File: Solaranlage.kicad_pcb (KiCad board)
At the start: 2 copper layers, 160 x 85 mm, 87 parts, among them J1 Screw_Terminal_01x02, J2 Screw_Terminal_01x02, J3 AVR-JTAG-10, J4 USB_B, J5 USB_B, J6 Screw_Terminal_01x02, Q1 2N3904, SW1 Rotary_Encoder_Switch_Panason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, SW2 SW_SPDT, U1 SC56-11E*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

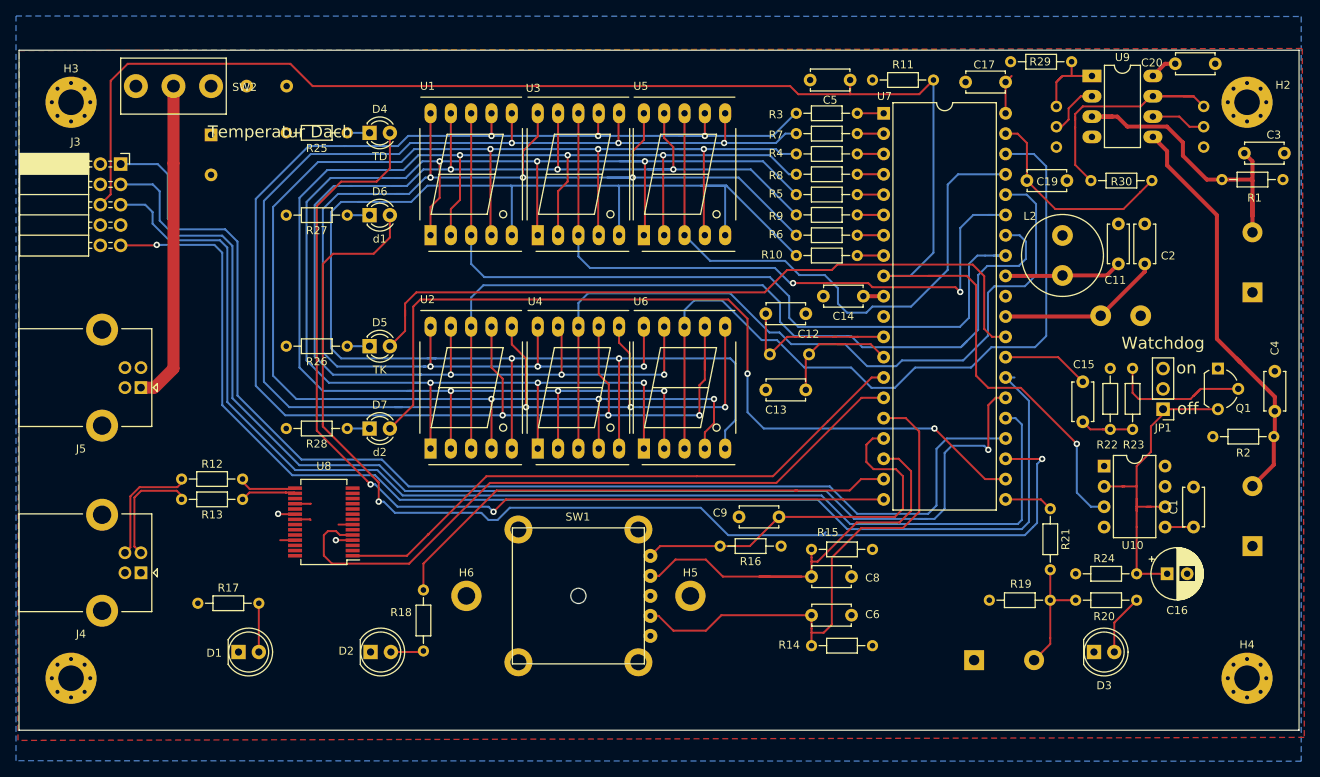
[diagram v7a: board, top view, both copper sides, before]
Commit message: adapted remarks from schematic review; added output buffer to PWM output
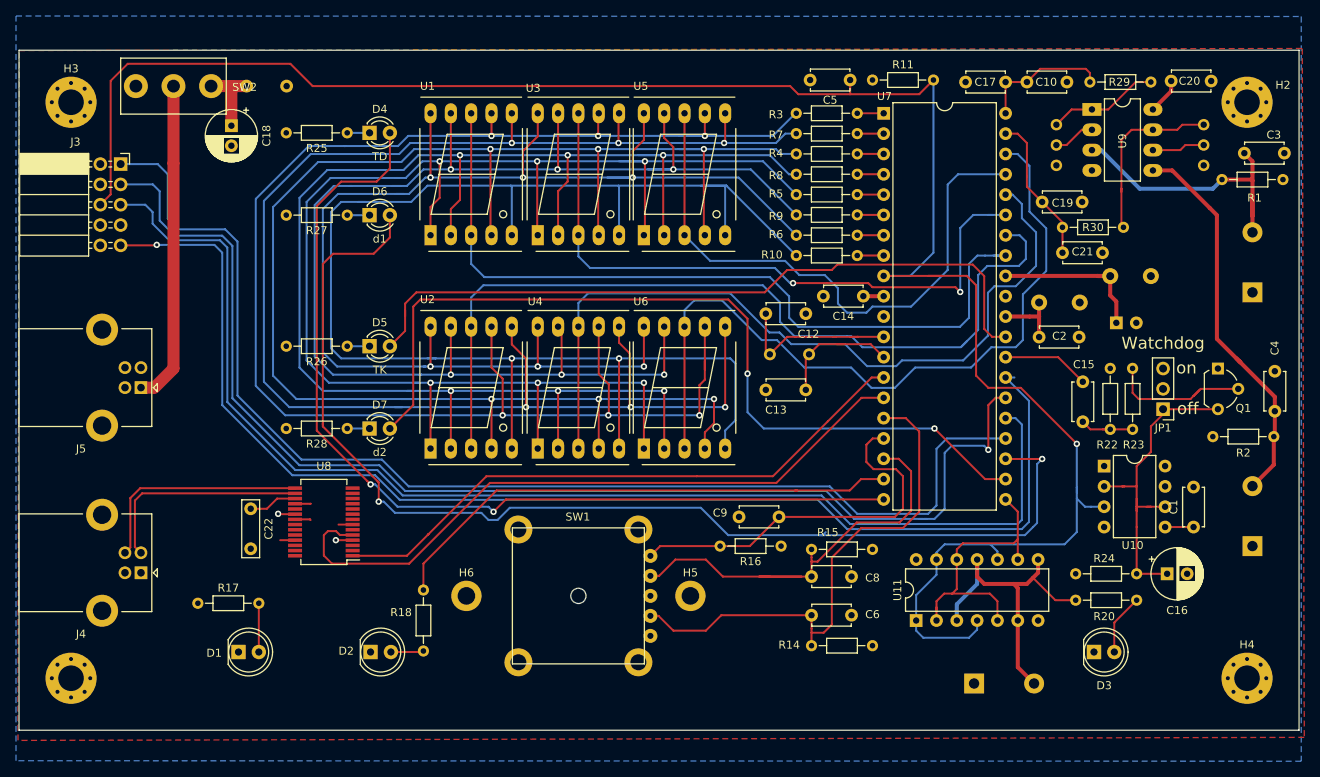
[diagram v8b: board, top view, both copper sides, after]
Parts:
- removed R12, R13: 22, Resistor_THT:R_Axial_DIN0204_L3.6mm_D1.6mm_P7.62mm_Horizontal
- removed R19: 10k, Resistor_THT:R_Axial_DIN0204_L3.6mm_D1.6mm_P7.62mm_Horizontal
- removed R21: 1k, Resistor_THT:R_Axial_DIN0204_L3.6mm_D1.6mm_P7.62mm_Horizontal
- added C10: 100n, Capacitor_THT:C_Disc_D4.7mm_W2.5mm_P5.00mm, F.Cu at (195.1, 59.2)
- added C21: 100n, Capacitor_THT:C_Disc_D4.7mm_W2.5mm_P5.00mm, F.Cu at (199.5, 80.5)
- added C22: 100n, Capacitor_THT:C_Rect_L7.0mm_W2.0mm_P5.00mm, F.Cu at (98.0, 112.5)
- added U11: 74LS125, Package_DIP:DIP-14_W7.62mm, F.Cu at (181.2, 126.5)
- C11: value 100n -> 13uF; footprint Capacitor_THT:C_Disc_D4.7mm_W2.5mm_P5.00mm -> Capacitor_THT:CP_Radial_D6.3mm_P2.50mm; moved to B.Cu
- C18: value 10u1 -> 13uF; footprint Capacitor_THT:CP_Radial_D8.0mm_P5.00mm -> Capacitor_THT:CP_Radial_D6.3mm_P2.50mm; moved to F.Cu
- L1: value INDUCTOR -> 10uH; footprint Inductor_THT:L_Radial_D10.0mm_P5.00mm_Fastron_07P -> Inductor_THT:L_Axial_L9.5mm_D4.0mm_P5.08mm_Vertical_Fastron_SMCC
- L2: value INDUCTOR -> 10u; footprint Inductor_THT:L_Radial_D10.0mm_P5.00mm_Fastron_07P -> Inductor_THT:L_Axial_L9.5mm_D4.0mm_P5.08mm_Vertical_Fastron_SMCC; moved to B.Cu
- moved C2 16.1 mm to (196.6, 91.1), turned to 0 degrees
- moved R30 12.6 mm to (199.5, 77.3), turned to 0 degrees
- moved L2 12.2 mm to (210.6, 83.4), turned to 180 degrees
- moved R29 10.2 mm to (202.9, 59.2)
- moved L1 7.80 mm to (201.7, 86.7)
- moved C11 7.37 mm to (206.2, 89.3), turned to 0 degrees
- moved U9 4.19 mm to (203.2, 62.6)
- moved C19 3.28 mm to (197.0, 74.2)
- moved J6 2.92 mm to (188.5, 134.4)
- moved C18 2.79 mm to (95.6, 64.6)
- moved RV1 2.29 mm to (198.8, 64.5)
- moved RV2 2.29 mm to (217.2, 64.5)
- moved C20 2.22 mm to (213.1, 59.1)
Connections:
- J6 pad 2: /PWM -> /PWM2
- R20 pad 1: /PWM -> /PWM2
- U7 pad 21: Net-(R21-Pad1) -> /PWM
- U8 pad 15: Net-(R12-Pad1) -> Net-(J4-Pad3)
- U8 pad 16: Net-(R13-Pad1) -> Net-(J4-Pad2)
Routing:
- net \RST: track 204.2 -> 250.7 mm
- net /PWM2: track 0.00 -> 41.0 mm
- net /PWM: track 15.3 -> 35.8 mm
- net /AVCC: track 27.0 -> 8.52 mm
- net Net-(J4-Pad3): track 14.9 -> 28.2 mm
- net Net-(J4-Pad2): track 14.2 -> 27.3 mm
- net /DACH_ADC: track 4.99 -> 16.5 mm
- net Net-(R30-Pad2): track 33.5 -> 22.5 mm
- net +5V: track 10.2 -> 20.8 mm
- net /KELLER_ADC: track 26.4 -> 18.7 mm
- net Net-(R12-Pad1): track 7.32 -> 0.00 mm
- net Net-(R13-Pad1): track 6.96 -> 0.00 mm
- net Net-(R21-Pad1): track 6.07 -> 0.00 mm
- net Net-(C22-Pad1): track 0.00 -> 6.07 mm
- net /AREF: track 15.3 -> 20.4 mm
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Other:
- board text removed: "Temperatur Dach"
